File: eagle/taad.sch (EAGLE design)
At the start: 44 parts, among them IC1 LD117AV33, Q1 16 MHz, X1 MINI-USB-32005-201

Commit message: Simplified schematic and made the SPI more like a bus. Updated components with new graphics and pinouts
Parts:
- removed GYRO/ACCEL: LSM330DLC, LSM330DLC:LSM330DLC
- removed WIRELESS_COMM: MRF24J40MA_TRANSEIVER_MODULE, MRF24J40MA:MRF24J40MA_TRANSEIVER_MODULE
- added U$2: LSM330DLC, LSM330DLC:LSM330DLC
- added U$3: MRF24J40MA_TRANSEIVER_MODULE, MRF24J40MA:MRF24J40MA_TRANSEIVER_MODULE
- C5: value 10n -> (none); device resistor:C-EU025-025X050 -> rcl:C-EUC0805
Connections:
- removed net CAP: C5.1, GYRO/ACCEL.CAP
- removed net N$10: GYRO/ACCEL.SDA_A/G, IC3G$1.DIN, MPU.PA13/PGMD1, WIRELESS_COMM.SDI
- removed net N$11: GYRO/ACCEL.CS_A, MPU.PA10/PGMM2
- removed net N$12: GYRO/ACCEL.CS_G, MPU.PA11/PGMM3
- removed net N$22: GYRO/ACCEL.SDO_A, GYRO/ACCEL.SDO_G, MPU.PA12/PGMD0, WIRELESS_COMM.SDO
- removed net N$7: MPU.PA5/PGMRDY, WIRELESS_COMM.CS
- removed net N$9: IC3G$1.CS, MPU.PA9/PGMM1
- removed net VCCIO: GYRO/ACCEL.VDD_IO
- new net N$34: C5.1, U$2.CAP
- new net NPCS0: MPU.PA11/PGMM3, U$2.CS_G
- new net NPCS1: MPU.PA9/PGMM1, U$3.CS
- new net NPCS2: MPU.PA10/PGMM2, U$2.CS_A
- new net NPCS3: IC3G$1.CS, MPU.PA5/PGMRDY
- new net SDA: IC3G$1.DIN, MPU.PA13/PGMD1, U$2.SDA_A/G, U$3.SDI
- new net SDO: MPU.PA12/PGMD0, U$2.SDO_A, U$2.SDO_G, U$3.SDO
- net +3V3: now also U$2.VDD, U$2.VDD_IO, U$3.VCC; no longer GYRO/ACCEL.RES_5, GYRO/ACCEL.RES_6, GYRO/ACCEL.RES_7, GYRO/ACCEL.RES_8, GYRO/ACCEL.RES_9, GYRO/ACCEL.VDD, GYRO/ACCEL.VDD_1, GYRO/ACCEL.VDD_2, WIRELESS_COMM.VIN
- net GND: now also U$2.GND, U$3.GND; no longer GYRO/ACCEL.GND, GYRO/ACCEL.GND_2, GYRO/ACCEL.RES_1, GYRO/ACCEL.RES_2, GYRO/ACCEL.RES_3, GYRO/ACCEL.RES_4, WIRELESS_COMM.GND_1, WIRELESS_COMM.GND_2, WIRELESS_COMM.GND_3
- net SCK: now also U$2.SCL_A/G, U$3.SCK; no longer GYRO/ACCEL.SCL_A/G, WIRELESS_COMM.SCK
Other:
- note added: "SCK"
- note added: "SDA"
- note added: "SDO"
- moved on the sheet: C1, C2, C3, C4, C5, IC1, IC3, JP1, JP10, JP11, JP12, JP13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

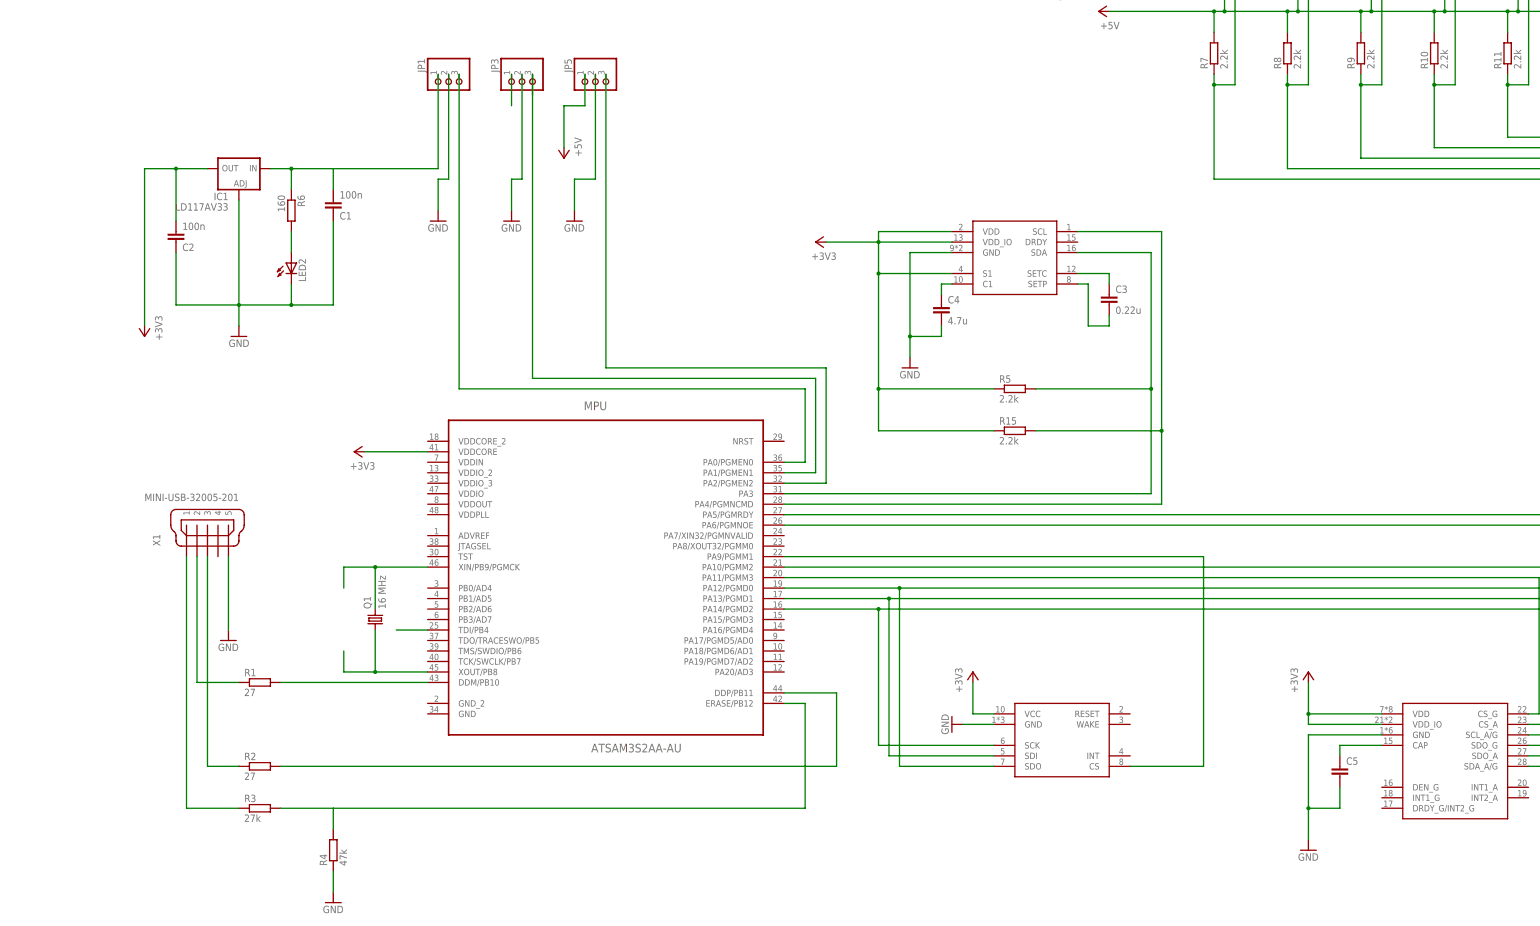
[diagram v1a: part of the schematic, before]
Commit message: Fixed powersupply to MPU
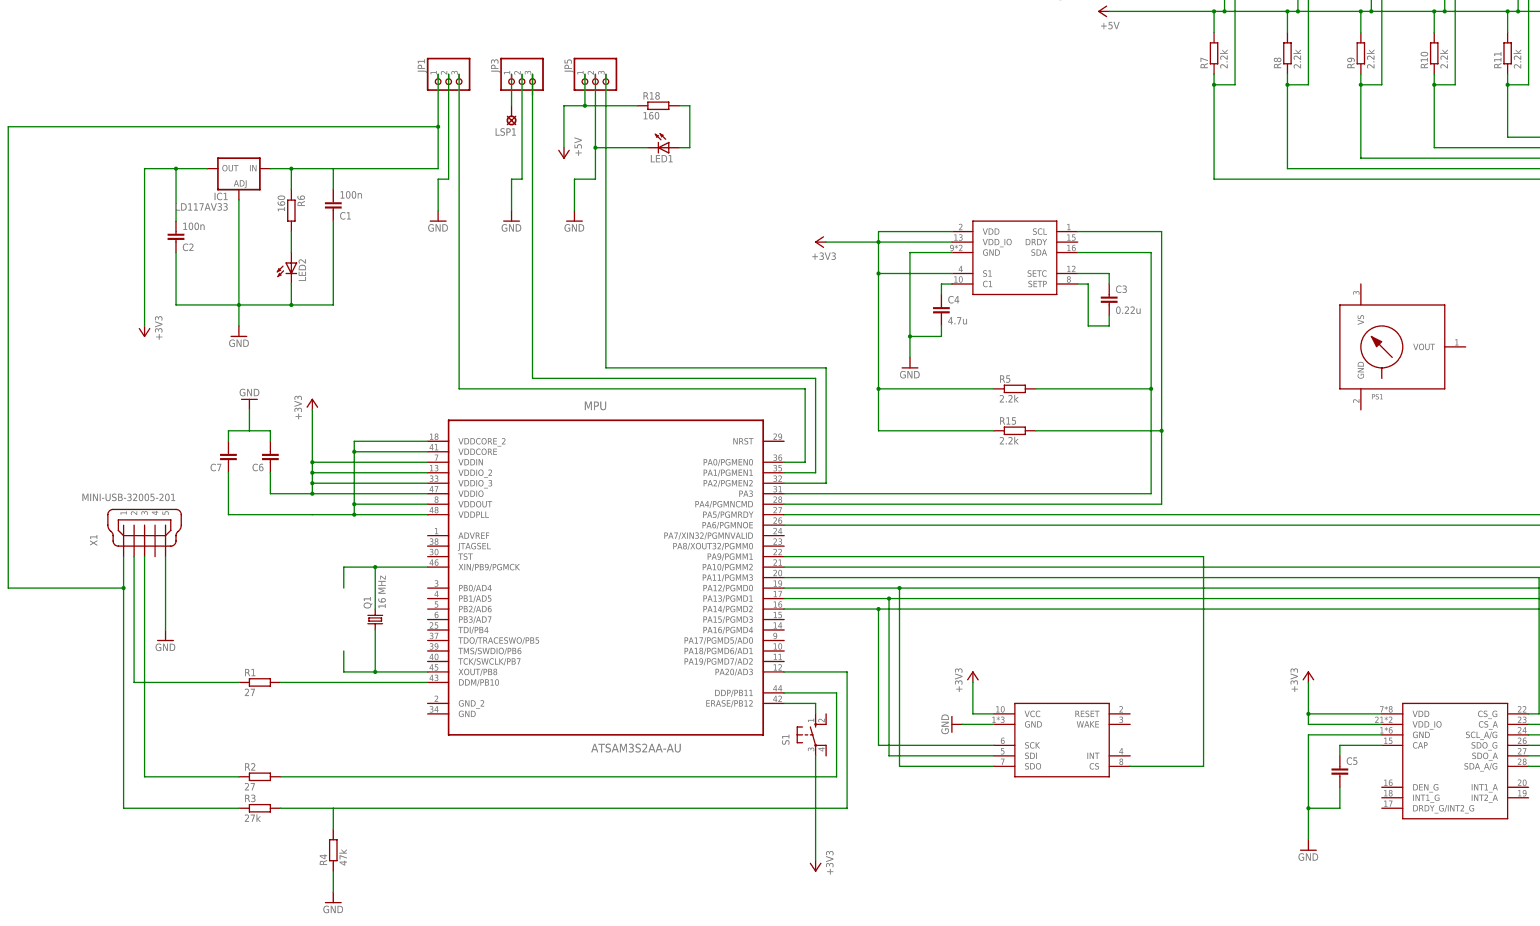
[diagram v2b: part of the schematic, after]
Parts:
- added C6, C7: (no value), rcl:C-EUC0805
- added LED1: (no value), led:LEDCHIP-LED0805
- added LSP1: LSP11, solpad:LSP11
- added PS1: (no value), mpx-freescale:MPX-867-H
- added R18: 160, resistor:R-EU_R0805
- added S1: (no value), switch-omron:10-XX
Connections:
- removed net N$35: MPU.TDI/PB4
- removed net N$6: C1.2, IC1.IN, JP1.1, R6.1
- new net N$10: MPU.ERASE/PB12, S1.S
- new net N$7: LED1.A, R18.2
- new net N$9: C7.1, MPU.VDDCORE, MPU.VDDCORE_2, MPU.VDDOUT, MPU.VDDPLL
- net +3V3: now also C6.1, MPU.VDDIN, MPU.VDDIO, MPU.VDDIO_2, MPU.VDDIO_3, S1.P; no longer MPU.VDDCORE
- net +5V: now also R18.1
- net GND: now also C6.2, C7.2, LED1.C
- net N$15: now also LSP1.MP
- net N$17: now also C1.2, IC1.IN, JP1.1, R6.1
- net N$18: now also MPU.PA20/AD3; no longer MPU.ERASE/PB12
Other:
- moved on the sheet: R2, X1

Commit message: More GPIO pins connected. Fixed VCC supply issues with USB. Etc etc etc
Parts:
- removed PS1: (no value), mpx-freescale:MPX-867-H
- removed U$2: LSM330DLC, LSM330DLC:LSM330DLC
- added C10, C9: 100n, rcl:C-EUC0805
- added C11, C8: 10µ, rcl:C-EUC0805
- added C12, C13: 10p, resistor:C-EUC0805
- added D1: 1N4148DO35-7, diode:1N4148DO35-7
- added GYRO/ACCEL: LSM330DLC, LSM330DLC:LSM330DLC
- added S2: (no value), switch-omron:10-XX
- C1, C2: device resistor:C-EU025-025X050 -> resistor:C-EUC0805
- C3: value 0.22u -> 0.22µ
- C4: value 4.7u -> 4.7µ
- C5: value (none) -> 10n
- C6: value (none) -> 10µ
- C7: value (none) -> 2.2µ
- renumbered IC3 to I/O-PWM, U$1 to COMPASS, U$3 to RF
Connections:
- new net DEN_G: GYRO/ACCEL.DEN_G, MPU.PA17/PGMD5/AD0
- new net INT1_A: GYRO/ACCEL.INT1_A, MPU.PA15/PGMD3
- new net INT1_G: GYRO/ACCEL.INT1_G, MPU.PA18/PGMD6/AD1
- new net INT2_A: GYRO/ACCEL.INT2_A, MPU.PA16/PGMD4
- new net INT2_G: GYRO/ACCEL.DRDY_G/INT2_G, MPU.PA19/PGMD7/AD2
- new net N$11: COMPASS.DRDY, MPU.PA7/XIN32/PGMNVALID
- new net N$24: C1.2, D1.C, IC1.IN, JP1.1, R6.1
- new net N$6: MPU.PA8/XOUT32/PGMM0, RF.INT
- new net RESET: MPU.NRST, RF.RESET, S2.S
- new net RF_WAKE: MPU.PB1/AD5, RF.WAKE
- net +3V3: now also C10.1, C11.1, C8.1, C9.1, GYRO/ACCEL.VDD, GYRO/ACCEL.VDD_IO, I/O-PWM.VDD; no longer U$2.VDD, U$2.VDD_IO
- net GND: now also C10.2, C11.2, C12.2, C13.2, C8.2, C9.2, GYRO/ACCEL.GND, I/O-PWM.GND, MPU.GND, MPU.GND_2; no longer U$2.GND
- net N$1: now also C12.1
- net N$13: now also I/O-PWM.P3; no longer I/O-PWMG$1.P3
- net N$14: now also I/O-PWM.OSC; no longer I/O-PWMG$1.OSC
- net N$17: now also D1.A; no longer C1.2, IC1.IN, JP1.1, R6.1
- net N$2: now also C13.1
- net N$23: now also I/O-PWM.P5; no longer I/O-PWMG$1.P5
- net N$26: now also I/O-PWM.P6; no longer I/O-PWMG$1.P6
- net N$27: now also I/O-PWM.P8; no longer I/O-PWMG$1.P8
- net N$28: now also I/O-PWM.P4; no longer I/O-PWMG$1.P4
- net N$34: now also GYRO/ACCEL.CAP; no longer U$2.CAP
- net N$36: now also I/O-PWM.P0; no longer I/O-PWMG$1.P0
- net N$37: now also I/O-PWM.P1; no longer I/O-PWMG$1.P1
- net N$38: now also I/O-PWM.P2; no longer I/O-PWMG$1.P2
- net N$39: now also I/O-PWM.P7; no longer I/O-PWMG$1.P7
- net N$8: now also I/O-PWM.P9; no longer I/O-PWMG$1.P9
- net N$9: now also S2.P
- net NPCS0: now also GYRO/ACCEL.CS_G; no longer U$2.CS_G
- net NPCS2: now also GYRO/ACCEL.CS_A; no longer U$2.CS_A
- net NPCS3: now also I/O-PWM.CS; no longer I/O-PWMG$1.CS
- net SCK: now also GYRO/ACCEL.SCL_A/G, I/O-PWM.SCLK; no longer I/O-PWMG$1.SCLK, U$2.SCL_A/G
- net SDA: now also GYRO/ACCEL.SDA_A/G, I/O-PWM.DIN; no longer I/O-PWMG$1.DIN, U$2.SDA_A/G
- net SDO: now also GYRO/ACCEL.SDO_A, GYRO/ACCEL.SDO_G; no longer U$2.SDO_A, U$2.SDO_G
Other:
- note added: "BEC connectors"
- note added: "PWM extender"
- note added: "RF"
- note added: "Servo connectors"
- note added: "USB"
- note added: "compass"
- note added: "gyro/accel"
- note added: "main voltage regulator"
- note removed: "SCK"
- note removed: "SDA"
- note removed: "SDO"
- moved on the sheet: C5, Q1, R1, R2, R3

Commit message: Board
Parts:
- removed JP1, JP12, JP13, JP3, JP5: (no value), pinhead:PINHD-1X3
- removed R10, R11, R12, R13, R14, R16, R17, R7, R8, R9: 2.2k, resistor:R-EU_R0805
- added ESC1_CONN, ESC2_CONN, ESC3_CONN: (no value), pinhead:PINHD-1X3/90
- added LED3, LED4, LED5, LED6, LED7, LED8: (no value), led:LEDCHIP-LED0805
- added R19, R20, R21, R22, R23, R24: 2.2k, resistor:R-EU_R0805
- added RN2, RN3: (no value), resistor-dil:4R-NEXBS8V
- IC1: value LD117AV33 -> LD117AS33TR; device v-reg:LD117AV33 -> v-reg:LD117AS33TR
- renumbered JP10 to SRV7_CONN, JP11 to SRV8_CONN, JP2 to SRV1_CONN, JP4 to SRV2_CONN, JP6 to SRV3_CONN, JP7 to SRV4_CONN, JP8 to SRV5_CONN, JP9 to SRV6_CONN
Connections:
- removed net N$27: I/O-PWM.P8, JP12.3, R16.1
- removed net N$6: MPU.PA8/XOUT32/PGMM0, RF.INT
- removed net N$8: I/O-PWM.P9, JP13.3, R17.1
- new net N$22: LED3.A, R19.1
- new net N$29: LED4.A, R20.1
- new net N$30: LED5.A, R21.1
- new net N$31: LED7.A, R23.1
- new net N$35: LED6.A, R22.1
- new net N$40: LED8.A, R24.1
- new net RF_INT: MPU.PA8/XOUT32/PGMM0, R24.2, RF.INT
- net +5V: now also ESC3_CONN.1, RN2A.2, RN2B.2, RN2C.2, RN2D.2, RN3A.2, RN3B.2, RN3C.2, RN3D.2; no longer JP12.2, JP13.2, JP5.1, R10.2, R11.2, R12.2, R13.2, R14.2, R16.2, R17.2, R7.2, R8.2, R9.2
- net ESC1: now also ESC1_CONN.3; no longer JP1.3
- net ESC2: now also ESC2_CONN.3; no longer JP3.3
- net ESC3: now also ESC3_CONN.3; no longer JP5.3
- net GND: now also ESC1_CONN.2, ESC2_CONN.2, ESC3_CONN.2, LED3.C, LED4.C, LED5.C, LED6.C, LED7.C, LED8.C; no longer JP1.2, JP12.1, JP13.1, JP3.2, JP5.2
- net N$13: now also RN2D.1; no longer R10.1
- net N$15: now also ESC2_CONN.1; no longer JP3.1
- net N$21: now also R19.2
- net N$23: now also RN3B.1; no longer R12.1
- net N$24: now also ESC1_CONN.1; no longer JP1.1
- net N$26: now also RN3C.1; no longer R13.1
- net N$28: now also RN3A.1; no longer R11.1
- net N$36: now also RN2A.1; no longer R7.1
- net N$37: now also RN2B.1; no longer R8.1
- net N$38: now also RN2C.1; no longer R9.1
- net N$39: now also RN3D.1; no longer R14.1
- net NPCS0: now also R22.2
- net NPCS1: now also R23.2
- net NPCS2: now also R21.2
- net NPCS3: now also R20.2

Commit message: Wired up everything except GND
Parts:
- removed C11, C8: 10µ, rcl:C-EUC0805
- removed C12, C13: 10p, resistor:C-EUC0805
- removed D1: 1N4148DO35-7, diode:1N4148DO35-7
- removed LED2, LED3, LED4, LED5, LED6, LED7, LED8: (no value), led:LEDCHIP-LED0805
- removed LSP1: LSP11, solpad:LSP11
- removed R1: 27, resistor:R-EU_R0805
- removed R19, R20, R21, R22, R23, R24: 2.2k, resistor:R-EU_R0805
- removed R4: 47k, resistor:R-EU_R0805
- removed R6: 160, resistor:R-EU_R0805
- removed RN3: (no value), resistor-dil:4R-NEXBS8V
- removed S2: (no value), switch-omron:10-XX
- removed SRV7_CONN, SRV8_CONN: (no value), pinhead:PINHD-1X3
- added ACC2, PWMC: 10µ, rcl:C-EUC0805
- added CC3: 0.1µ, rcl:C-EUC0805
- added JP1: (no value), pinhead:PINHD-1X4
- added JP2: (no value), pinhead:PINHD-2X8
- added JP4: (no value), pinhead:PINHD-1X8
- added LED_3V3: (no value), led:LEDCHIP-LED0805
- added RESET: (no value), switch-omron:10-XX
- added RN1: 2.2k, resistor-dil:4R-NEXB38V
- added R_3V3: 160, resistor:R-EU_R0805
- added USBD: (no value), diode:DIODE-SOD123
- added USBR3: 27k, resistor:R-EU_R0805
- added USBR4: 47k, resistor:R-EU_R0805
- added XINC, XOUTC: 10p, resistor:C-EUC0805
- ESC1_CONN, ESC2_CONN, ESC3_CONN: device pinhead:PINHD-1X3/90 -> pinhead:PINHD-1X3
- RN2: value (none) -> 2.2k; device resistor-dil:4R-NEXBS8V -> resistor-dil:4R-NEXB38V
- USBR2: value 27k -> 27
- renumbered C1 to LDOC1, C10 to ACC3, C2 to LDOC2, C3 to CC1, C4 to CC2, C5 to ACC4, C6 to CPUC2, C7 to CPUC1, C9 to ACC1, LED1 to LED_5V, R15 to TWI_CR, R18 to R_5V, R2 to USBR1, R3 to USBR2, R5 to TWI_DR, S1 to ERASE
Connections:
- net N$11 renamed COMPASS_DATA_READY
- net N$14 renamed PWM_CLOCK
- net N$19 renamed TWI_CLOCK
- removed net N$1: C12.1, MPU.XIN/PB9/PGMCK, Q1.2
- removed net N$13: I/O-PWM.P3, RN2D.1, SRV4_CONN.3
- removed net N$15: ESC2_CONN.1, LSP1.MP
- removed net N$16: MPU.DDM/PB10, R1.2
- removed net N$17: D1.A, USBR2.1, X1.1
- removed net N$18: MPU.PA20/AD3, R4.2, USBR2.2
- removed net N$2: C13.1, MPU.XOUT/PB8, Q1.1
- removed net N$20: LED2.A, R6.2
- removed net N$21: COMPASS.SDA, MPU.PA3, R19.2, TWI_DR.2
- removed net N$22: LED3.A, R19.1
- removed net N$23: I/O-PWM.P5, RN3B.1, SRV6_CONN.3
- removed net N$26: I/O-PWM.P6, RN3C.1, SRV7_CONN.3
- removed net N$28: I/O-PWM.P4, RN3A.1, SRV5_CONN.3
- removed net N$29: LED4.A, R20.1
- removed net N$30: LED5.A, R21.1
- removed net N$31: LED7.A, R23.1
- removed net N$35: LED6.A, R22.1
- removed net N$36: I/O-PWM.P0, RN2A.1, SRV1_CONN.3
- removed net N$37: I/O-PWM.P1, RN2B.1, SRV2_CONN.3
- removed net N$38: I/O-PWM.P2, RN2C.1, SRV3_CONN.3
- removed net N$39: I/O-PWM.P7, RN3D.1, SRV8_CONN.3
- removed net N$40: LED8.A, R24.1
- removed net N$9: CPUC1.1, MPU.VDDCORE, MPU.VDDCORE_2, MPU.VDDOUT, MPU.VDDPLL, S2.P
- new net AD0: JP4.3, MPU.PA17/PGMD5/AD0
- new net AD1: JP4.2, MPU.PA18/PGMD6/AD1
- new net AD2: JP4.1, MPU.PA19/PGMD7/AD2
- new net AD3: JP4.7, MPU.PB0/AD4
- new net AD4: JP4.6, MPU.PB1/AD5
- new net AD5: JP4.5, MPU.PB2/AD6
- new net AD6: JP4.4, MPU.PB3/AD7
- new net ADVREF: JP4.8, MPU.ADVREF
- new net DDM: MPU.DDM/PB10, USBR1.2
- new net DDP: MPU.DDP/PB11, USBR2.2
- new net IO1: I/O-PWM.P6, JP1.1, RN2C.1
- new net IO2: I/O-PWM.P7, JP1.2, RN2B.1
- new net IO3: I/O-PWM.P9, JP1.3
- new net IO4: I/O-PWM.P4, JP1.4
- new net SRV1: I/O-PWM.P0, RN1D.1, SRV1_CONN.3
- new net SRV2: I/O-PWM.P1, RN1C.1, SRV2_CONN.3
- new net SRV3: I/O-PWM.P2, RN1B.1, SRV3_CONN.3
- new net SRV4: I/O-PWM.P3, RN1A.1, SRV4_CONN.3
- new net SRV5: I/O-PWM.P8, RN2A.1, SRV5_CONN.3
- new net SRV6: I/O-PWM.P5, RN2D.1, SRV6_CONN.3
- new net TWI_DATA: COMPASS.SDA, MPU.PA3, TWI_DR.2
- new net USB+5V: USBD.A, USBR3.1, X1.1
- new net USB_CONNECTED: MPU.PA20/AD3, USBR3.2, USBR4.2
- new net VDDCORE: CPUC1.1, MPU.VDDCORE, MPU.VDDCORE_2, MPU.VDDOUT, MPU.VDDPLL
- new net XIN: MPU.XIN/PB9/PGMCK, Q1.2, XINC.1
- new net XOUT: MPU.XOUT/PB8, Q1.1, XOUTC.1
- net +3V3: now also ACC2.1, CC3.2, JP2.1, JP2.3, JP2.5, JP2.7, PWMC.1; no longer C11.1, C8.1, ERASE.P
- net +5V: now also JP2.11, JP2.13, JP2.15, JP2.9, RN1A.2, RN1B.2, RN1C.2, RN1D.2; no longer RN3A.2, RN3B.2, RN3C.2, RN3D.2, SRV7_CONN.2, SRV8_CONN.2
- net DEN_G: now also MPU.TCK/SWCLK/PB7; no longer MPU.PA17/PGMD5/AD0
- net GND: now also ACC2.2, CC3.1, ERASE.P, JP2.10, JP2.12, JP2.14, JP2.16, JP2.2, JP2.4, JP2.6, JP2.8, PWMC.2, RESET.S1, R_3V3.2, USBR4.1, XINC.2, XOUTC.2; no longer C11.2, C12.2, C13.2, C8.2, LED2.C, LED3.C, LED4.C, LED5.C, LED6.C, LED7.C, LED8.C, R4.1, SRV7_CONN.1, SRV8_CONN.1
- net INT1_G: now also MPU.TDO/TRACESWO/PB5; no longer MPU.PA18/PGMD6/AD1
- net INT2_G: now also MPU.TMS/SWDIO/PB6; no longer MPU.PA19/PGMD7/AD2
- net N$24: now also LED_3V3.A, USBD.C; no longer D1.C, R6.1
- net N$3: now also USBR2.1; no longer USBR1.1
- net N$4: now also USBR1.1; no longer R1.1
- net N$5: now also LED_3V3.C, R_3V3.1; no longer MPU.DDP/PB11, USBR1.2
- net NPCS0: now also GYRO/ACCEL.CS_A; no longer GYRO/ACCEL.CS_G, R22.2
- net NPCS1: no longer R23.2
- net NPCS2: now also GYRO/ACCEL.CS_G; no longer GYRO/ACCEL.CS_A, R21.2
- net NPCS3: no longer R20.2
- net RESET: now also RESET.P1; no longer S2.S
- net RF_INT: no longer R24.2
- net RF_WAKE: now also MPU.TDI/PB4; no longer MPU.PB1/AD5
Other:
- moved on the sheet: Q1, RN2A, RN2B, RN2C, RN2D, X1

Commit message: Updated with recommendations from Hannes regarding capacitors on supply and some diagnostic leds. New routing of components
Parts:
- removed CPUC1: 2.2µ, rcl:C-EUC0805
- removed CPUC2: 10µ, rcl:C-EUC0805
- added CPUIN1, CPUIN2, CPUIN3, CPUIN4, CPUOUT1: 100n, rcl:C-EUC0805
- added CPUIN5: 10µ, rcl:C-EUC0805
- added CPUOUT2: 2.2µ, rcl:C-EUC0805
- added JP3: (no value), pinhead:PINHD-1X5
- added LED_3V1, LED_3V2: (no value), led:LEDCHIP-LED0805
- added R_3V1, R_3V2: 160, resistor:R-EU_R0805
- added USBD1: (no value), diode:DIODE-SOD123
- JP4: device pinhead:PINHD-1X8 -> pinhead:PINHD-1X1
- Q1: device crystal:CRYSTALHC49S -> crystal:CRYSTALHC49UP; OC_FARNELL (none) -> unknown
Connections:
- removed net AD0: JP4.3, MPU.PA17/PGMD5/AD0
- removed net AD1: JP4.2, MPU.PA18/PGMD6/AD1
- removed net AD2: JP4.1, MPU.PA19/PGMD7/AD2
- new net N$1: ESC1_CONN.1, USBD1.A
- new net N$11: JP4.1, MPU.TDO/TRACESWO/PB5
- new net N$2: LED_3V2.A, MPU.TMS/SWDIO/PB6
- new net N$6: LED_3V1.A, MPU.TCK/SWCLK/PB7
- new net N$8: LED_3V2.C, R_3V1.1
- new net N$9: LED_3V1.C, R_3V2.1
- net +3V3: now also CPUIN1.2, CPUIN2.2, CPUIN3.2, CPUIN4.2, CPUIN5.1, ERASE.P; no longer CPUC2.1
- net AD3: now also JP3.4; no longer JP4.7
- net AD4: now also JP3.3; no longer JP4.6
- net AD5: now also JP3.2; no longer JP4.5
- net AD6: now also JP3.1; no longer JP4.4
- net ADVREF: now also JP3.5; no longer JP4.8
- net DEN_G: now also MPU.PA19/PGMD7/AD2; no longer MPU.TCK/SWCLK/PB7
- net ESC1: now also MPU.PA1/PGMEN1; no longer MPU.PA0/PGMEN0
- net ESC2: now also MPU.PA0/PGMEN0; no longer MPU.PA1/PGMEN1
- net GND: now also CPUIN1.1, CPUIN2.1, CPUIN3.1, CPUIN4.1, CPUIN5.2, CPUOUT1.2, CPUOUT2.2, R_3V1.2, R_3V2.2; no longer CPUC1.2, CPUC2.2, ERASE.P
- net INT1_G: now also MPU.PA17/PGMD5/AD0; no longer MPU.TDO/TRACESWO/PB5
- net INT2_G: now also MPU.PA18/PGMD6/AD1; no longer MPU.TMS/SWDIO/PB6
- net N$24: now also USBD1.C; no longer ESC1_CONN.1
- net NPCS0: now also GYRO/ACCEL.CS_G; no longer GYRO/ACCEL.CS_A
- net NPCS2: now also GYRO/ACCEL.CS_A; no longer GYRO/ACCEL.CS_G
- net VDDCORE: now also CPUOUT1.1, CPUOUT2.1; no longer CPUC1.1
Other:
- moved on the sheet: USBR4
